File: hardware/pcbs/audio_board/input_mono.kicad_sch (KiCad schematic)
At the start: 10 parts, among them J9 AudioJack3

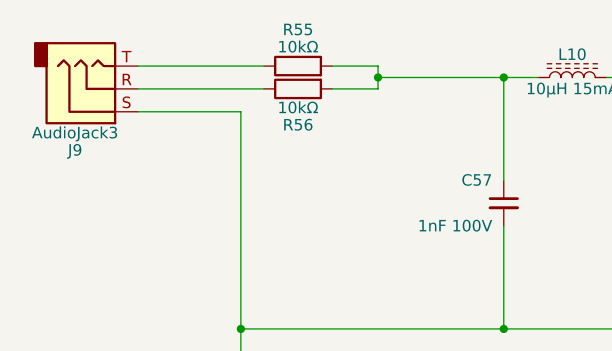
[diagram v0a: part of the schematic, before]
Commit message: Colored netclasses and added lables
- added colored netclasses to easier differentiate analog/digital/power
  lines
- added netnames to previously unnamed nets:
  - PC Mono Input AudioJack3 J9: OUT+T and OUT+R for the nets behind the
    resistors
  - root page: MOSI_R, SCK_R, CS_RIGHT_R, CS_LEFT_R for the nets behind
    the resistors so that the SPI lines can be colored accordingly
- use slightly different colors on PCB to not get blinded when looking
  at it

No functional changes, only cosmetics and net lables.
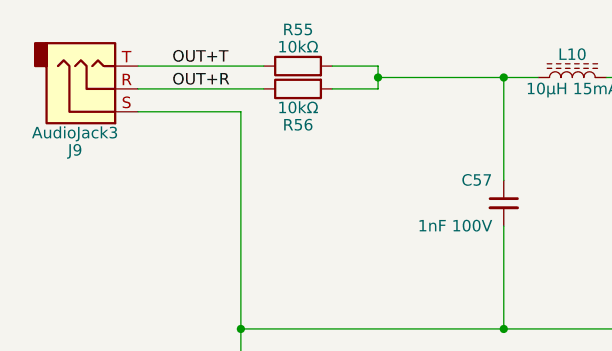
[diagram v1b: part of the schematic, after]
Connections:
- net OUT+T: now reaches J9.T, R55.1
- net OUT+R: now reaches J9.R, R56.1
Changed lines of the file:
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@@
+		)
+	)
+	(label "OUT+R"
+		(at 91.44 96.52 0)
+		(effects
+			(font
+				(size 1.27 1.27)
+			)
+			(justify left bottom)
+		)
+	)
+	(label "OUT+T"
+		(at 91.44 93.98 0)
+		(effects
+			(font
+				(size 1.27 1.27)
+			)
+			(justify left bottom)
 		)
 	)
